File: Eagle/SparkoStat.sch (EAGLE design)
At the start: 30 parts, among them IC1 MIC4680-5.0YM, K1 AQY282EHA, K2 AQY282EHA, K3 AQY282EHA, K4 AQY282EHA, Q1 NPN

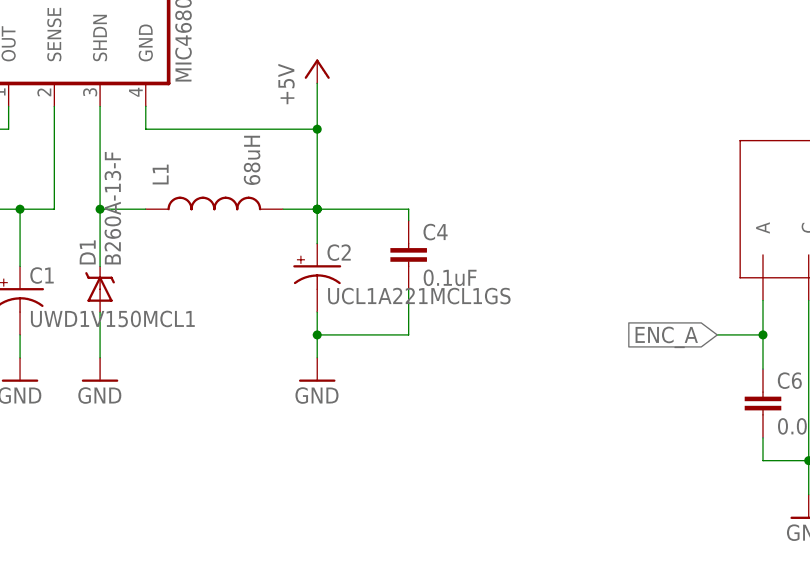
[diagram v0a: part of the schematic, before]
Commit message: Changed DHT22 to verticle
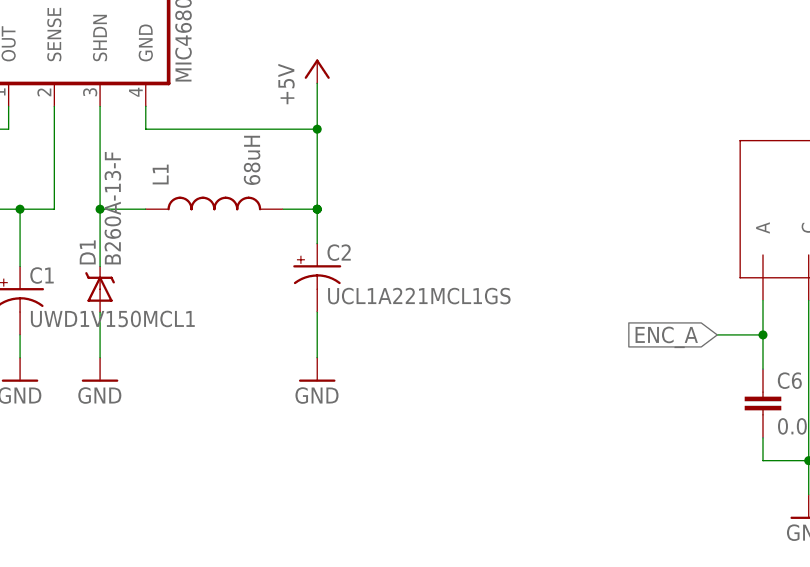
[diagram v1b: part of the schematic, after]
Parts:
- removed C4: 0.1uF, SparkFun-Capacitors:CAP0805
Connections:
- net +5V: no longer C4.1
- net GND: no longer C4.2
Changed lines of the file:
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@@
 <?xml version="1.0" encoding="utf-8"?>
 <!DOCTYPE eagle SYSTEM "eagle.dtd">
-<eagle version="7.1.0">
+<eagle version="7.3.0">
 <drawing>
 <settings>
@@
 <part name="R5" library="SparkFun-Passives" deviceset="RESISTOR" device="0805-RES" value="200"/>
 <part name="C3" library="SparkFun-Capacitors" deviceset="CAP" device="0805" value="0.1uF"/>
-<part name="C4" library="SparkFun-Capacitors" deviceset="CAP" device="0805" value="0.1uF"/>
 <part name="SJ1" library="jumper" deviceset="SJ" device=""/>
 <part name="C5" library="SparkFun-Capacitors" deviceset="CAP" device="0805" value="0.01uF"/>
@@
 <instance part="R5" gate="G$1" x="212.09" y="106.68" rot="R180"/>
 <instance part="C3" gate="G$1" x="224.79" y="119.38"/>
-<instance part="C4" gate="G$1" x="116.84" y="120.65"/>
 <instance part="SJ1" gate="1" x="43.18" y="25.4" rot="R90"/>
 <instance part="C5" gate="G$1" x="166.37" y="104.14"/>
@@
 <segment>
 <pinref part="GND11" gate="1" pin="GND"/>
-<wire x1="106.68" y1="110.49" x2="106.68" y2="113.03" width="0.1524" layer="91"/>
 <pinref part="C2" gate="G$1" pin="-"/>
-<pinref part="C4" gate="G$1" pin="2"/>
-<wire x1="106.68" y1="113.03" x2="106.68" y2="115.57" width="0.1524" layer="91"/>
-<wire x1="106.68" y1="113.03" x2="116.84" y2="113.03" width="0.1524" layer="91"/>
-<wire x1="116.84" y1="113.03" x2="116.84" y2="118.11" width="0.1524" layer="91"/>
-<junction x="106.68" y="113.03"/>
+<wire x1="106.68" y1="110.49" x2="106.68" y2="115.57" width="0.1524" layer="91"/>
 </segment>
 <segment>
@@
 <pinref part="C2" gate="G$1" pin="+"/>
 <pinref part="L1" gate="G$1" pin="2"/>
-<wire x1="106.68" y1="127" x2="116.84" y2="127" width="0.1524" layer="91"/>
-<pinref part="C4" gate="G$1" pin="1"/>
-<wire x1="116.84" y1="127" x2="116.84" y2="125.73" width="0.1524" layer="91"/>
-</segment>
-<segment>
+</segment>
+<segment>
